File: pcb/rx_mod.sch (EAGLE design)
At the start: 25 parts, among them U1 ATMEGA328

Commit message: diversity ready version - TESTED
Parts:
- removed 3157: TS5A3157, pimoroni:TS5A3157
- removed ICSP1: 3x2 M, SmartPrj:PINHD-2X3
- removed OLED: (no value), pinhead:PINHD-1X4
- removed R_LED: 330, rcl:R-US_R0603
- removed R_PD_SWITCH: 10K, rcl:R-US_R0805
- removed STATUS: (no value), led:LEDSML0603
- added C3: (no value), adafruit:C-USC0603
- added JP3: (no value), SparkFun-Connectors:M07
- added JP4: (no value), SparkFun-Connectors:M04PTH
- added LED_1, LED_2: (no value), led:LEDSML0603
- added R_LED1, R_LED2: 330, rcl:R-US_R0603
- added R_RSSI1: 100K, SparkFun:RESISTOR0603-RES
- added U2: (no value), ts5a3359:TS5A3359
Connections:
- net SPI_SEL renamed SPI_SEL_A
- removed net LED_PIN: STATUS.A, U1.ADC7
- new net N$11: LED_2.C, R_LED2.1
- new net RSSI_B: JP3.5, R_RSSI1.2, U1.PC1(ADC1)
- new net RXVIDOUT2: JP3.4, U2.NO0
- new net SPI_SEL_B: JP3.2, U1.PB0(ICP)
- new net SW_CTRL2: LED_2.A, U1.PD6(AIN0), U2.IN2
- net 5V: now also C3.1, JP3.7, U2.VCC; no longer 3157.VCC, ICSP1.2, OLED.4
- net GND: now also C3.2, JP3.6, R_LED1.2, R_LED2.2, R_RSSI1.1, U2.GND; no longer 3157.GND, ICSP1.6, OLED.3, R_LED.2, R_PD_SWITCH.1
- net MISO: now also JP4.3; no longer ICSP1.1
- net MOSI: now also JP4.2; no longer ICSP1.4
- net N$3: now also LED_1.C, R_LED1.1; no longer R_LED.1, STATUS.C
- net N$6: now also U2.COM; no longer RECEIVER_A.VIDEO
- net OSD_VOUT: now also U2.NO2; no longer 3157.NO
- net RESET: now also JP4.1; no longer ICSP1.5
- net RXVIDOUT: now also RECEIVER_A.VIDEO, U2.NO1; no longer 3157.NC, C2.-, R_VIDOUT.2
- net SCK: now also JP4.4; no longer ICSP1.3
- net SCL: no longer OLED.2
- net SDA: no longer OLED.1
- net SPI_CLK: now also JP3.3
- net SPI_DATA: now also JP3.1
- net SW_CTRL: now also LED_1.A, U2.IN1; no longer 3157.IN, R_PD_SWITCH.2
- net VIDOUT: now also C2.-, R_VIDOUT.2; no longer 3157.COM
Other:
- moved on the sheet: C1, C2, C_AREF, C_DTR, C_VIN, JP1, JP2, R_CLK, R_PU_RST, R_RSSI, R_SPIDATA, R_SPI_SEL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

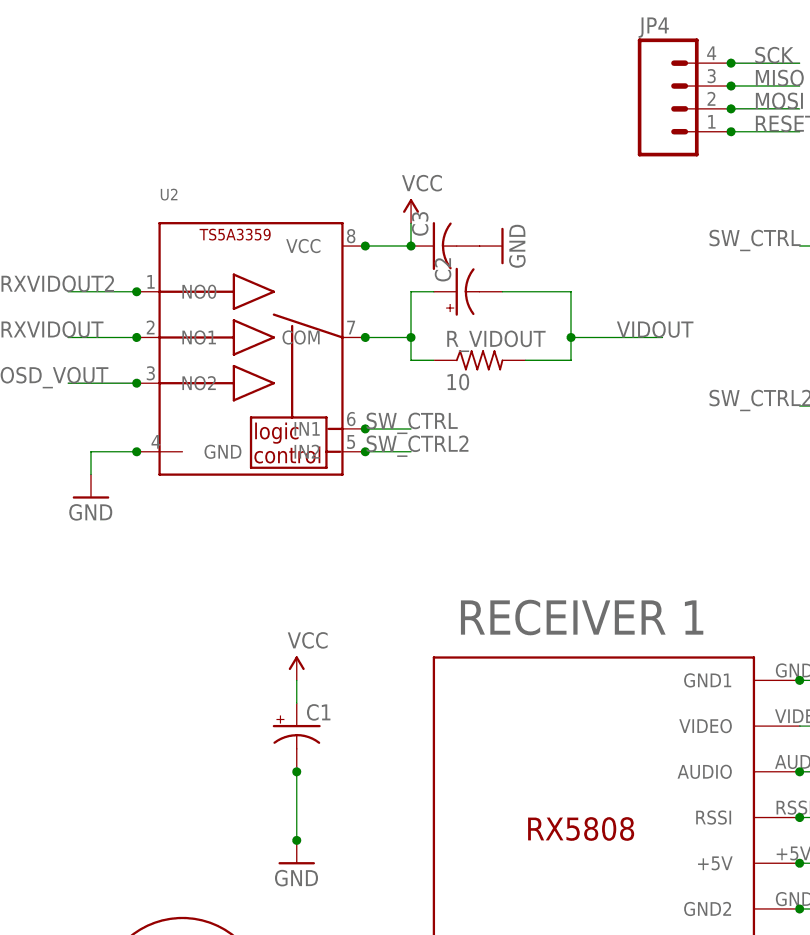
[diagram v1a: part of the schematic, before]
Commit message: new SMA connetor
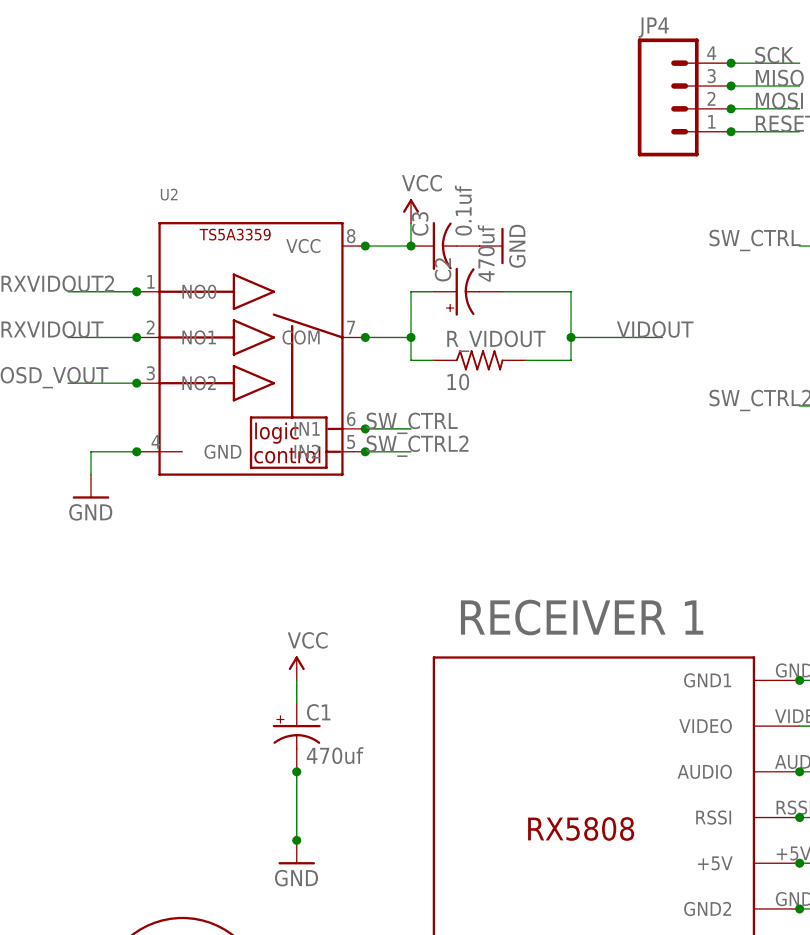
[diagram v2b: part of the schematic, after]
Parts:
- C1, C2: value (none) -> 470uf
- C3: value (none) -> 0.1uf
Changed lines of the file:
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@@
 <?xml version="1.0" encoding="utf-8"?>
 <!DOCTYPE eagle SYSTEM "eagle.dtd">
-<eagle version="7.4.0">
+<eagle version="7.5.0">
 <drawing>
 <settings>
@@
 <part name="XTAL1" library="CSTCE16M0V53-R0" deviceset="CSTCE16M0V53-R0" device=""/>
 <part name="U$1" library="#fpv" deviceset="SMA_ANTENNA" device=""/>
-<part name="C1" library="SparkFun-Passives" deviceset="CAP_POL" device="7343"/>
-<part name="C2" library="SparkFun-Passives" deviceset="CAP_POL" device="7343"/>
+<part name="C1" library="SparkFun-Passives" deviceset="CAP_POL" device="7343" value="470uf"/>
+<part name="C2" library="SparkFun-Passives" deviceset="CAP_POL" device="7343" value="470uf"/>
 <part name="P+8" library="SparkFun" deviceset="3.3V" device="" value="VCC"/>
 <part name="GND16" library="supply1" deviceset="GND" device=""/>
@@
 <part name="R_LED2" library="rcl" deviceset="R-US_" device="R0603" value="330"/>
 <part name="LED_2" library="led" deviceset="LED" device="SML0603"/>
-<part name="C3" library="adafruit" deviceset="C-US" device="C0603"/>
+<part name="C3" library="adafruit" deviceset="C-US" device="C0603" value="0.1uf"/>
 <part name="GND18" library="supply1" deviceset="GND" device=""/>
 </parts>
